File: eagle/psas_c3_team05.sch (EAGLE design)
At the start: 80 parts, among them IC1 CP2102, Q1 32 MHz, U1 MIC5219 3.3V, U2 MCP73871

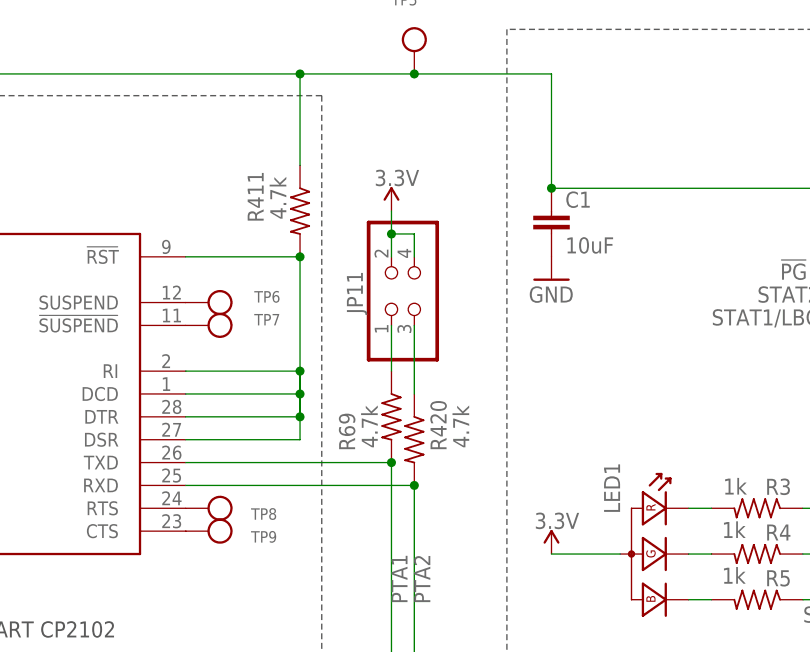
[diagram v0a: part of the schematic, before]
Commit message: Layout reconfig and got rid of sch component
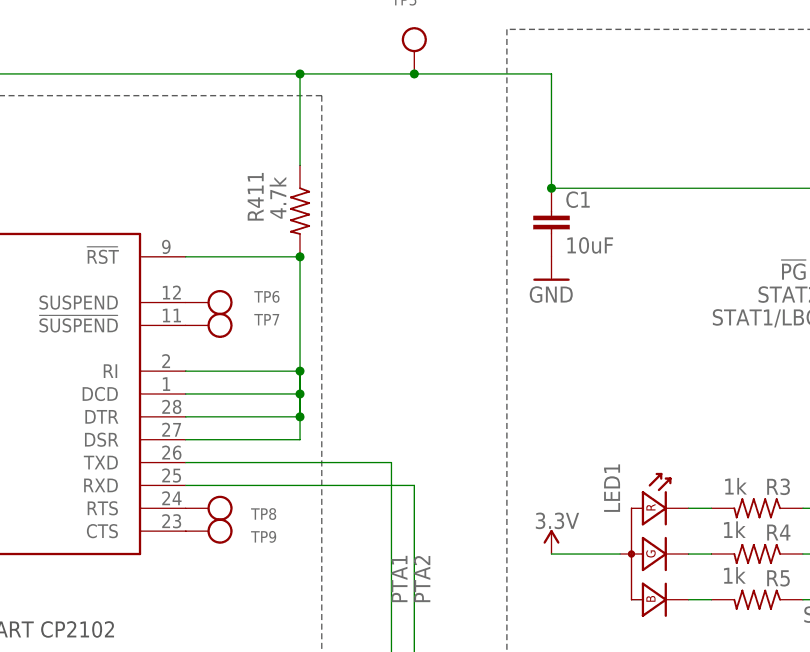
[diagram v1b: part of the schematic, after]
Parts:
- removed JP11: (no value), pinhead:PINHD-2X2
- removed R420, R69: 4.7k, rcl_custom:R-US_0603-B-NOSILK
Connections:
- removed net N$28: JP11.1, R69.1
- removed net N$29: JP11.3, R420.1
- net 3.3V: no longer JP11.2, JP11.4
- net PTA1: no longer R69.2
- net PTA2: no longer R420.2
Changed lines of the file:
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@@
 <part name="JP9" library="pinhead" deviceset="PINHD-2X3" device=""/>
 <part name="JP10" library="pinhead" deviceset="PINHD-2X8" device=""/>
-<part name="R420" library="rcl_custom" deviceset="R-US_" device="0603-B-NOSILK" value="4.7k"/>
-<part name="R69" library="rcl_custom" deviceset="R-US_" device="0603-B-NOSILK" value="4.7k"/>
-<part name="JP11" library="pinhead" deviceset="PINHD-2X2" device=""/>
-<part name="P+9" library="Vibrogait_prototype" deviceset="3.3V" device=""/>
 <part name="GND14" library="Vibrogait_prototype" deviceset="GND" device=""/>
 <part name="TP12" library="microbuilder" deviceset="TESTPOINT" device="ROUND0.5MM"/>
@@
 <instance part="JP9" gate="A" x="233.68" y="330.2"/>
 <instance part="JP10" gate="A" x="373.38" y="157.48"/>
-<instance part="R420" gate="R" x="180.34" y="314.96" smashed="yes" rot="R270">
-<attribute name="NAME" x="183.9214" y="313.69" size="1.778" layer="95" rot="R90"/>
-<attribute name="VALUE" x="184.658" y="318.77" size="1.778" layer="96" rot="R270"/>
-</instance>
-<instance part="R69" gate="R" x="177.8" y="317.5" smashed="yes" rot="R270">
-<attribute name="NAME" x="173.7614" y="313.69" size="1.778" layer="95" rot="R90"/>
-<attribute name="VALUE" x="174.498" y="318.77" size="1.778" layer="96" rot="R270"/>
-</instance>
-<instance part="JP11" gate="A" x="180.34" y="332.74" smashed="yes" rot="R90">
-<attribute name="NAME" x="174.625" y="328.93" size="1.778" layer="95" rot="R90"/>
-<attribute name="VALUE" x="185.42" y="323.85" size="1.778" layer="96" rot="R90"/>
-</instance>
-<instance part="P+9" gate="G$1" x="177.8" y="340.36" smashed="yes">
-<attribute name="VALUE" x="175.895" y="343.154" size="1.778" layer="96"/>
-</instance>
 <instance part="GND14" gate="1" x="269.24" y="198.12"/>
 <instance part="TP12" gate="G$1" x="60.96" y="314.96" smashed="yes" rot="R180">
@@
 <junction x="309.88" y="213.36"/>
 <junction x="309.88" y="226.06"/>
-</segment>
-<segment>
-<pinref part="JP11" gate="A" pin="2"/>
-<pinref part="P+9" gate="G$1" pin="3.3V"/>
-<wire x1="177.8" y1="340.36" x2="177.8" y2="337.82" width="0.1524" layer="91"/>
-<pinref part="JP11" gate="A" pin="4"/>
-<wire x1="177.8" y1="337.82" x2="177.8" y2="335.28" width="0.1524" layer="91"/>
-<wire x1="177.8" y1="337.82" x2="180.34" y2="337.82" width="0.1524" layer="91"/>
-<wire x1="180.34" y1="337.82" x2="180.34" y2="335.28" width="0.1524" layer="91"/>
-<junction x="177.8" y="337.82"/>
 </segment>
 </net>
@@
 <wire x1="378.46" y1="162.56" x2="370.84" y2="162.56" width="0.1524" layer="91"/>
 <junction x="370.84" y="162.56"/>
-<pinref part="R69" gate="R" pin="2"/>
-<junction x="177.8" y="312.42"/>
 </segment>
 </net>
@@
 <wire x1="378.46" y1="160.02" x2="370.84" y2="160.02" width="0.1524" layer="91"/>
 <junction x="370.84" y="160.02"/>
-<pinref part="R420" gate="R" pin="2"/>
 <pinref part="IC1" gate="G$1" pin="RXD"/>
 <wire x1="154.94" y1="309.88" x2="180.34" y2="309.88" width="0.1524" layer="91"/>
-<junction x="180.34" y="309.88"/>
 </segment>
 </net>
@@
 </segment>
 </net>
-<net name="N$29" class="0">
-<segment>
-<pinref part="R420" gate="R" pin="1"/>
-<pinref part="JP11" gate="A" pin="3"/>
-<wire x1="180.34" y1="320.04" x2="180.34" y2="327.66" width="0.1524" layer="91"/>
-</segment>
-</net>
-<net name="N$28" class="0">
-<segment>
-<pinref part="R69" gate="R" pin="1"/>
-<pinref part="JP11" gate="A" pin="1"/>
-<wire x1="177.8" y1="322.58" x2="177.8" y2="327.66" width="0.1524" layer="91"/>
-</segment>
-</net>

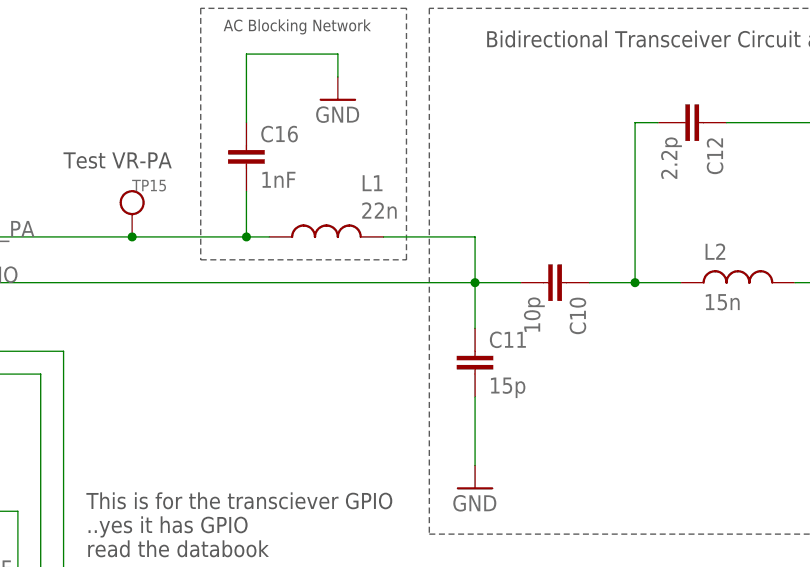
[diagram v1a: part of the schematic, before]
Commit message: Changed values for RF
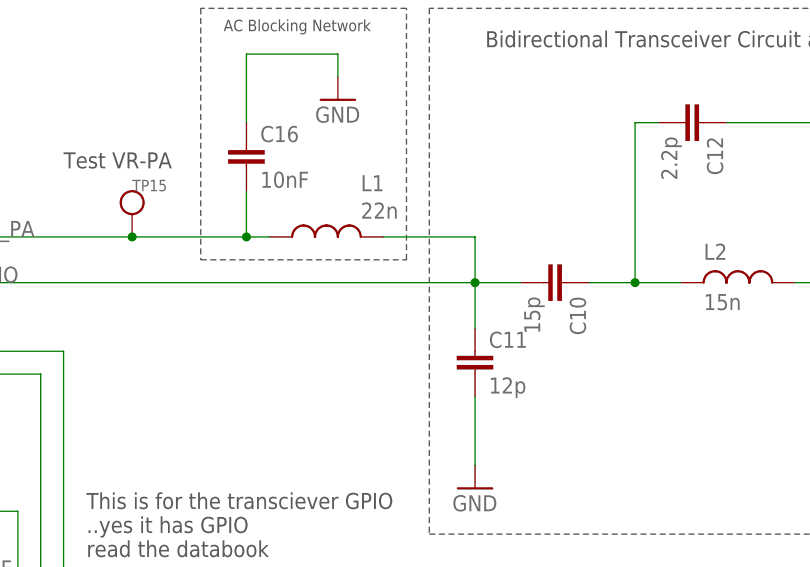
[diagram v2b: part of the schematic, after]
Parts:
- C10: value 10p -> 15p
- C11: value 15p -> 12p
- C16: value 1nF -> 10nF
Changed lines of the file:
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@@
 <part name="CF1" library="Vibrogait_prototype" deviceset="CON_USB-MICRO-B-RECEPTACLE-*" device="PTH-HIROSE-ZX62D-B-5P8" value="CF1"/>
 <part name="JP2" library="SparkFun-v5" deviceset="M02" device="PTH"/>
-<part name="C10" library="rcl_custom" deviceset="C-EU" device="0603-B-NOSILK" value="10p"/>
-<part name="C11" library="rcl_custom" deviceset="C-EU" device="0603-B-NOSILK" value="15p"/>
+<part name="C10" library="rcl_custom" deviceset="C-EU" device="0603-B-NOSILK" value="15p"/>
+<part name="C11" library="rcl_custom" deviceset="C-EU" device="0603-B-NOSILK" value="12p"/>
 <part name="C12" library="rcl_custom" deviceset="C-EU" device="0603-B-NOSILK" value="2.2p"/>
 <part name="C13" library="rcl_custom" deviceset="C-EU" device="0603-B-NOSILK" value="15p"/>
@@
 <part name="GND19" library="Vibrogait_prototype" deviceset="GND" device=""/>
 <part name="C15" library="rcl_custom" deviceset="C-EU" device="0603-B-NOSILK" value="100nF"/>
-<part name="C16" library="rcl_custom" deviceset="C-EU" device="0603-B-NOSILK" value="1nF"/>
+<part name="C16" library="rcl_custom" deviceset="C-EU" device="0603-B-NOSILK" value="10nF"/>
 <part name="GND20" library="Vibrogait_prototype" deviceset="GND" device=""/>
 <part name="L1" library="rcl_custom" deviceset="L-US" device="0603-B-NOSILK" value="22n"/>

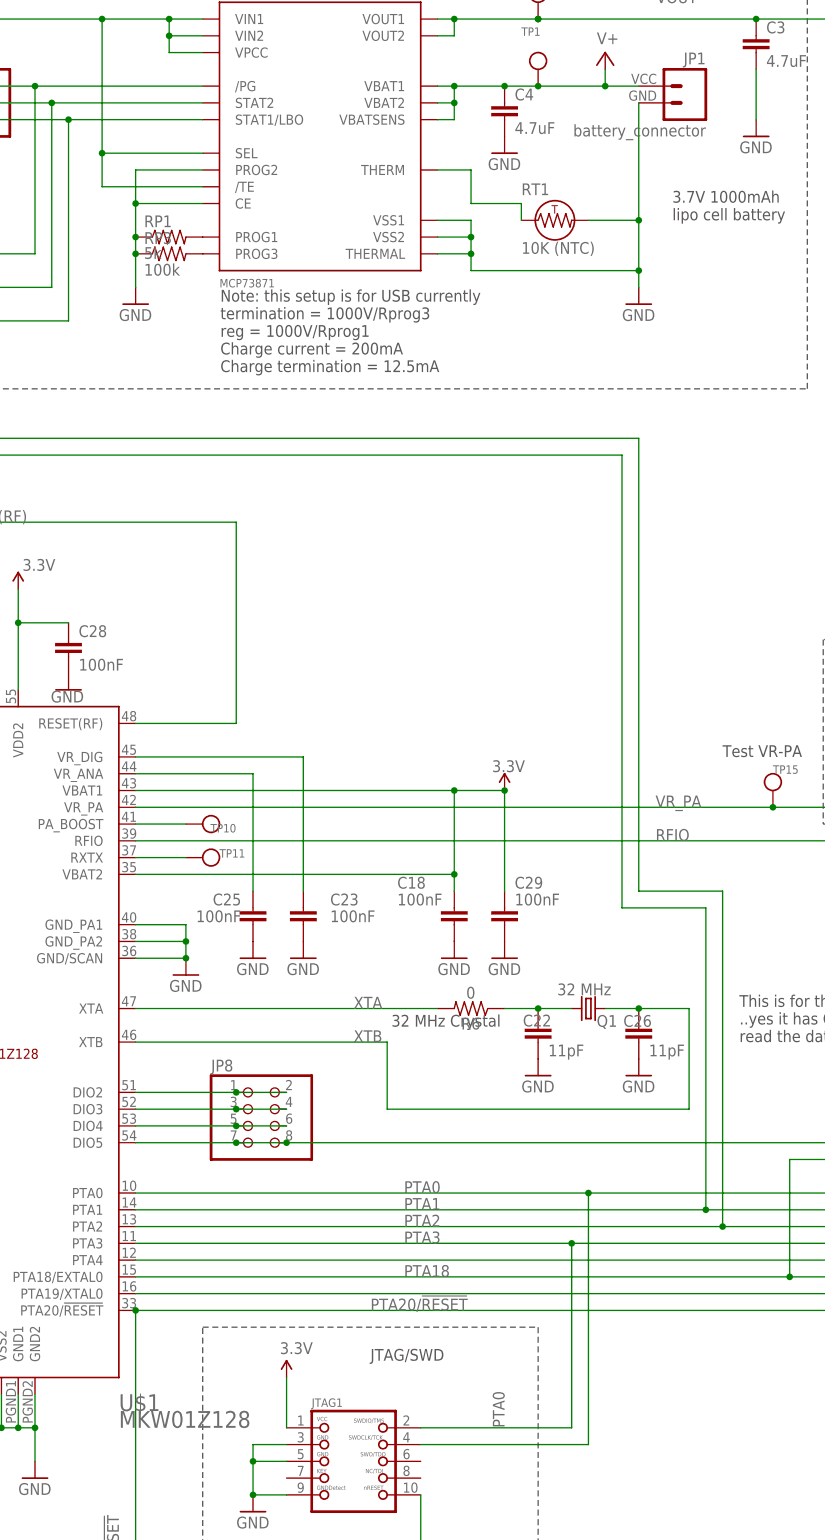
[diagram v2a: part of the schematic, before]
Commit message: Adjusted the position of labels, and added missing boader
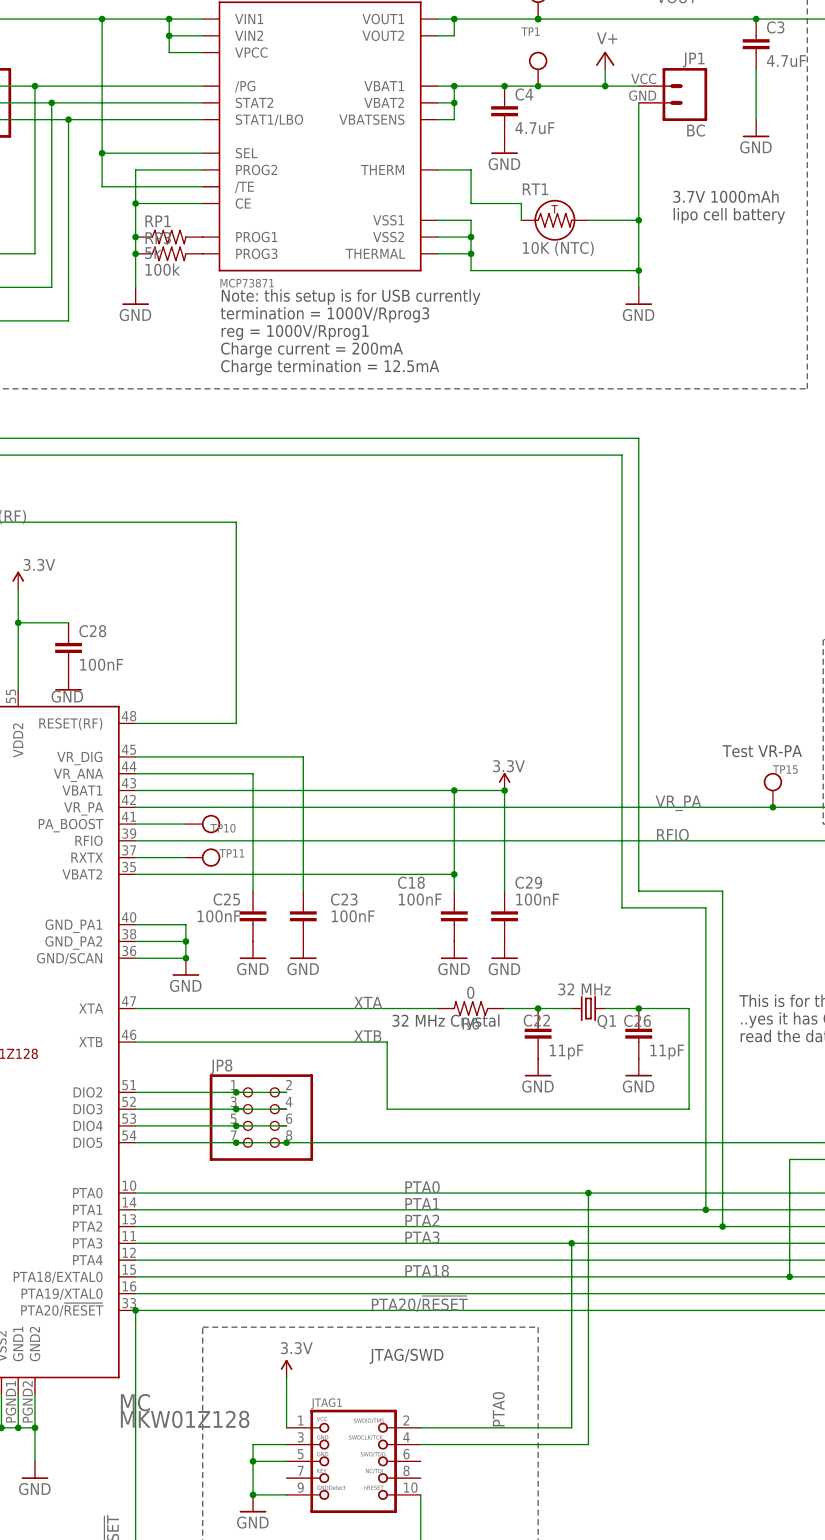
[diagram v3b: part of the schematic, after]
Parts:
- JP1: value battery_connector -> BC
- renumbered U$1 to MC

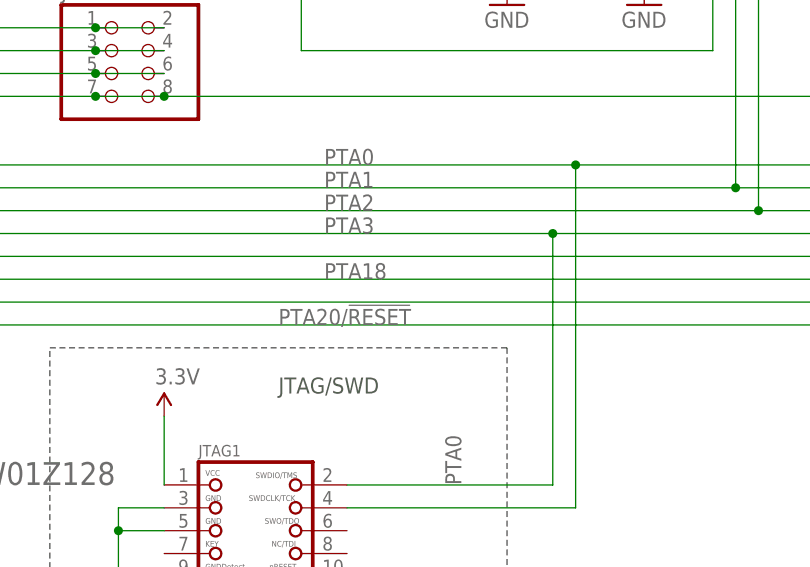
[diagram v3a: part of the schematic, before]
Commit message: added labels for MCU ports on board layout, labeled some lines on PORTA of MCU that were missing labels
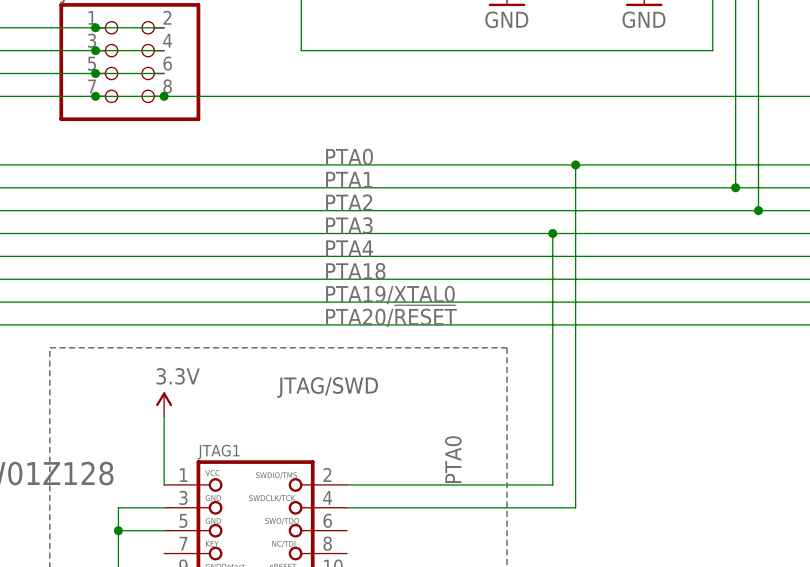
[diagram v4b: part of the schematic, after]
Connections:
- net N$26 renamed PTA4
- net N$27 renamed PTA19/XTAL0
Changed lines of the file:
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@@
 <?xml version="1.0" encoding="utf-8"?>
 <!DOCTYPE eagle SYSTEM "eagle.dtd">
-<eagle version="7.4.0">
+<eagle version="7.3.0">
 <drawing>
 <settings>
@@
 <layer number="91" name="Nets" color="2" fill="1" visible="yes" active="yes"/>
 <layer number="92" name="Busses" color="1" fill="1" visible="yes" active="yes"/>
-<layer number="93" name="Pins" color="2" fill="1" visible="yes" active="yes"/>
+<layer number="93" name="Pins" color="2" fill="1" visible="no" active="yes"/>
 <layer number="94" name="Symbols" color="4" fill="1" visible="yes" active="yes"/>
 <layer number="95" name="Names" color="7" fill="1" visible="yes" active="yes"/>
@@
 <wire x1="304.8" y1="119.38" x2="304.8" y2="109.22" width="0.1524" layer="91"/>
 <wire x1="304.8" y1="109.22" x2="261.62" y2="109.22" width="0.1524" layer="91"/>
-<label x="297.18" y="147.32" size="1.778" layer="95"/>
+<label x="302.26" y="147.32" size="1.778" layer="95"/>
 <wire x1="261.62" y1="109.22" x2="261.62" y2="81.28" width="0.1524" layer="91"/>
 <junction x="261.62" y="109.22"/>
@@
 </segment>
 </net>
-<net name="N$26" class="0">
+<net name="PTA4" class="0">
 <segment>
 <pinref part="MC" gate="G$1" pin="PTA4"/>
@@
 <wire x1="378.46" y1="154.94" x2="370.84" y2="154.94" width="0.1524" layer="91"/>
 <junction x="370.84" y="154.94"/>
-</segment>
-</net>
-<net name="N$27" class="0">
+<label x="302.26" y="154.94" size="1.778" layer="95"/>
+</segment>
+</net>
+<net name="PTA19/XTAL0" class="0">
 <segment>
 <pinref part="MC" gate="G$1" pin="PTA19/XTAL0"/>
@@
 <wire x1="378.46" y1="149.86" x2="370.84" y2="149.86" width="0.1524" layer="91"/>
 <junction x="370.84" y="149.86"/>
-</segment>
-</net>
+<label x="302.26" y="149.86" size="1.778" layer="95"/>
+</segment>
+</net>

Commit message: General schematic clean a la Andrew -- Cap sizes, CP2102 test points and unused chips, killed VBUS diode, added power LED, Added TBG LED for KW0x that still needs to be connected, Misc OCD cleanup.
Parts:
- removed D1: (no value), Vibrogait_prototype:DIODE_SCHOTTKY_1N5819
- removed Q1: 32 MHz, crystal:FC-12M
- added JP11: (no value), pinhead:PINHD-1X2
- added LED2: APHFT1612PBASURKVGAC, Vibrogait_prototype:LED_RGB_COMMON_ANODE-1.6X1.26
- added LED3: GRN, Vibrogait_prototype:LED-0603
- added R2, R7, R8, R9: 1k, rcl_custom:R-US_0603-B-NOSILK
- added TP13, TP14, TP16, TP17, TP18: (no value), microbuilder:TESTPOINTROUND0.5MM
- added X1: 32 MHz, crystal:FC-12M
- C1: value 10uF -> 4.7uF; device rcl_custom:C-EU0603-B-NOSILK -> rcl_custom:C-EU0805-B-NOSILK
- C3, C4: device rcl_custom:C-EU0603-B-NOSILK -> rcl_custom:C-EU0805-B-NOSILK
- C6: value 4.7uF -> 2.2uF; device rcl_custom:C-EU0603-B-NOSILK -> rcl_custom:C-EU0805-B-NOSILK
- LED1: value (none) -> APHFT1612PBASURKVGAC
- U1: value MIC5219 3.3V -> MIC5319 3.3V
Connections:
- net N$34 renamed SHIELD
- new net N$26: IC1.DTR, TP9.P$1
- new net N$27: IC1.DCD, TP16.P$1
- new net N$28: IC1.DSR, TP17.P$1
- new net N$29: IC1.CTS, TP18.P$1
- new net N$31: LED3.K, R2.2
- net !PG: now also R4.1; no longer R3.1
- net 3.3V: now also LED3.A
- net GND: now also JP11.2, R2.1; no longer D1.ANODE
- net N$12: now also X1.2; no longer Q1.2
- net N$24: now also R411.1, TP13.P$1
- net N$25: now also IC1.RI, TP14.P$1; no longer IC1.CTS, TP9.P$1
- net N$30: now also JP11.1; no longer IC1.DCD, IC1.DSR, IC1.DTR, IC1.RI
- net STAT2: now also R3.1; no longer R4.1
- net VBUS: no longer D1.CATHODE, R411.1
- net XTB: now also X1.1; no longer Q1.1
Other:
- note removed: "32 MHz Crystal"
- note removed: "Avalanche transient voltage suppression diodes for ESD protection"
- note removed: "SHIELD"
- note removed: "This is for the transciever GPIO ..yes it has GPIO read the databook"
- note removed: "VBUS"
- moved on the sheet: C1, C11, C12, C13, C14, C15, C17, C2, C20, C26, C3, C4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
